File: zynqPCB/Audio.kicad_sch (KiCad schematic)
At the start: 67 parts, among them J2 AUDIO JACK, J3 AUDIO JACK, J4 AUDIO JACK, J5 JACK_TRS_4PINS, Q1 IRLML2502, Q2 IRLML2502, Q3 IRLML2502, Q4 IRLML2502, Q5 IRLML2502, Q6 IRLML2502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

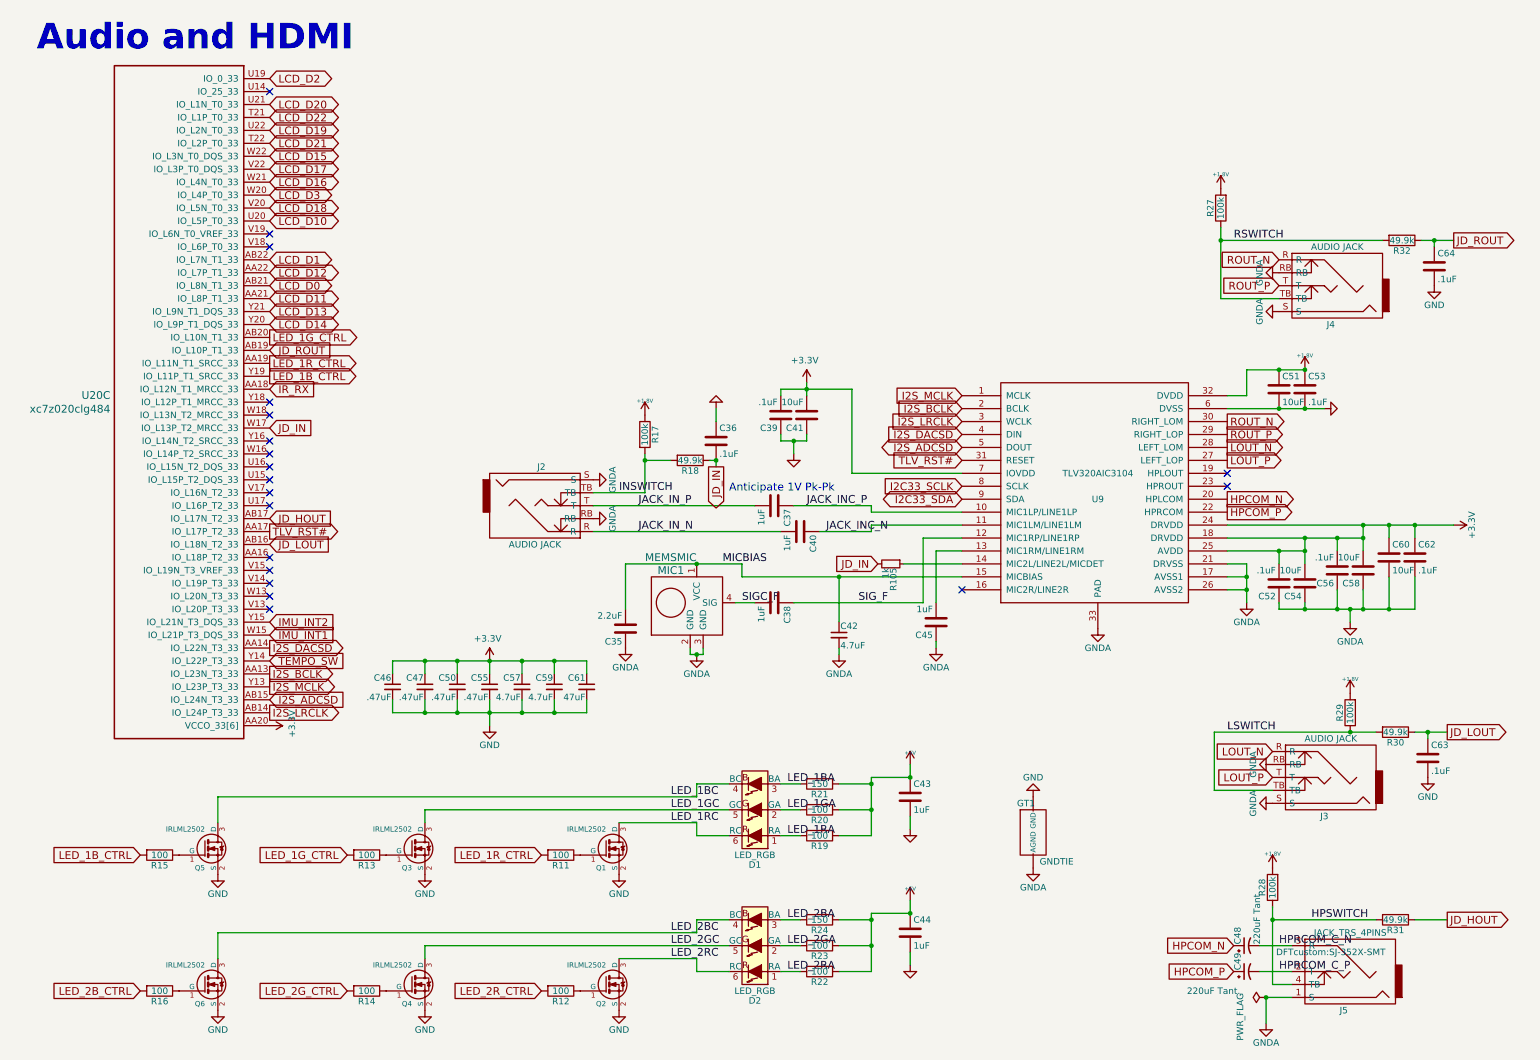
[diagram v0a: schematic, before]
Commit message: Update audio schematic
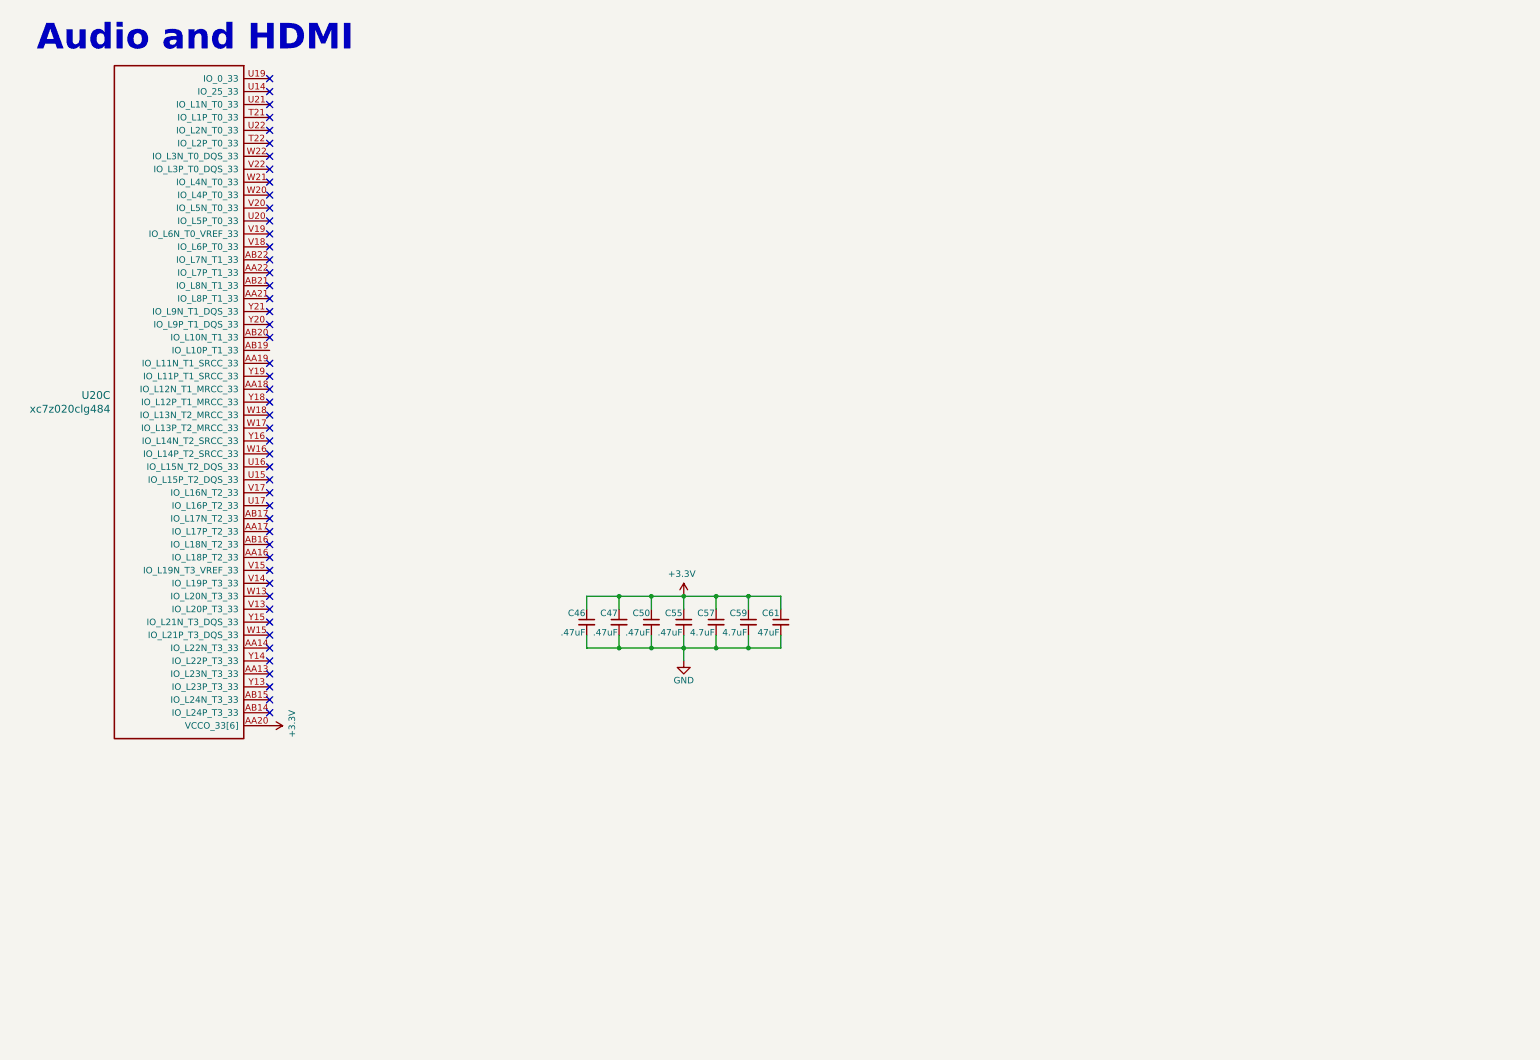
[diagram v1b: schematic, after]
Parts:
- removed C35: 2.2uF, Capacitor_SMD:C_0402_1005Metric, symbol Device:C
- removed C36, C39, C52, C53, C56, C62, C63, C64: .1uF, Capacitor_SMD:C_0402_1005Metric, symbol Device:C
- removed C37, C38, C40, C43, C44, C45: 1uF, Capacitor_SMD:C_0402_1005Metric, symbol Device:C
- removed C41, C51, C54, C58, C60: 10uF, Capacitor_SMD:C_0603_1608Metric, symbol Device:C
- removed C42: 4.7uF, Capacitor_SMD:C_0402_1005Metric, symbol Device:C_Small
- removed C48, C49: 220uF Tant., Capacitor_Tantalum_SMD:CP_EIA-3528-12_Kemet-T, symbol Device:CP1_Small
- removed D1, D2: LED_RGB, DFTcustom:PLCC6-SM-RGB-LED, symbol DFTBoard-rescue:LED_RGB-RESCUE-DFTBoard-
- removed GT1: GNDTIE, DFTcustom:gndtie, symbol DFTBoard-rescue:GNDTIE-
- removed J2, J3, J4: AUDIO JACK, DFTcustom:RA49C14B, symbol DFTBoard-rescue:JACK_TRS_5PINS
- removed J5: JACK_TRS_4PINS, DFTcustom:SJ-352X-SMT, symbol DFTBoard-rescue:JACK_TRS_4PINS
- removed MIC1: MEMSMIC, SPW2430HR5H-B:MIC_SPW2430HR5H-B, symbol DFTBoard-rescue:MEMSMIC
- removed Q1, Q2, Q3, Q4, Q5, Q6: IRLML2502, Package_TO_SOT_SMD:SOT-23, symbol DFTBoard-rescue:IRLML2502-
- removed R105: 1k, Resistor_SMD:R_0402_1005Metric, symbol Device:R_Small
- removed R11, R12, R13, R14, R15, R16, R19, R20, R22, R23: 100, Resistor_SMD:R_0402_1005Metric, symbol Device:R
- removed R17, R27, R28, R29: 100k, Resistor_SMD:R_0402_1005Metric, symbol Device:R
- removed R18, R30, R31, R32: 49.9k, Resistor_SMD:R_0402_1005Metric, symbol Device:R
- removed R21, R24: 150, Resistor_SMD:R_0402_1005Metric, symbol Device:R
- removed U9: TLV320AIC3104, Package_DFN_QFN:QFN-32-1EP_5x5mm_P0.5mm_EP3.65x3.65mm, symbol DFTBoard-rescue:TLV320AIC3104
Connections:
- net I2S_ADCSD: no longer names the net of U20.AB15 (IO_L24N_T3_33)
- net I2S_BCLK: no longer names the net of U20.AA13 (IO_L23N_T3_33)
- net I2S_DACSD: no longer names the net of U20.AA14 (IO_L22N_T3_33)
- net I2S_LRCLK: no longer names the net of U20.AB14 (IO_L24P_T3_33)
- net I2S_MCLK: no longer names the net of U20.Y13 (IO_L23P_T3_33)
- net IMU_INT1: no longer names the net of U20.W15 (IO_L21P_T3_DQS_33)
- net IMU_INT2: no longer names the net of U20.Y15 (IO_L21N_T3_DQS_33)
- net IR_RX: no longer names the net of U20.AA18 (IO_L12N_T1_MRCC_33)
- net JD_HOUT: no longer names the net of U20.AB17 (IO_L17N_T2_33)
- net JD_IN: no longer names the net of U20.W17 (IO_L13P_T2_MRCC_33)
- net JD_LOUT: no longer names the net of U20.AB16 (IO_L18N_T2_33)
- net JD_ROUT: no longer names the net of U20.AB19 (IO_L10P_T1_33)
- net LCD_D0: no longer names the net of U20.AB21 (IO_L8N_T1_33)
- net LCD_D1: no longer names the net of U20.AB22 (IO_L7N_T1_33)
- net LCD_D10: no longer names the net of U20.U20 (IO_L5P_T0_33)
- net LCD_D11: no longer names the net of U20.AA21 (IO_L8P_T1_33)
- net LCD_D12: no longer names the net of U20.AA22 (IO_L7P_T1_33)
- net LCD_D13: no longer names the net of U20.Y21 (IO_L9N_T1_DQS_33)
- net LCD_D14: no longer names the net of U20.Y20 (IO_L9P_T1_DQS_33)
- net LCD_D15: no longer names the net of U20.W22 (IO_L3N_T0_DQS_33)
- net LCD_D16: no longer names the net of U20.W21 (IO_L4N_T0_33)
- net LCD_D17: no longer names the net of U20.V22 (IO_L3P_T0_DQS_33)
- net LCD_D18: no longer names the net of U20.V20 (IO_L5N_T0_33)
- net LCD_D19: no longer names the net of U20.U22 (IO_L2N_T0_33)
- net LCD_D2: no longer names the net of U20.U19 (IO_0_33)
- net LCD_D20: no longer names the net of U20.U21 (IO_L1N_T0_33)
- net LCD_D21: no longer names the net of U20.T22 (IO_L2P_T0_33)
- net LCD_D22: no longer names the net of U20.T21 (IO_L1P_T0_33)
- net LCD_D3: no longer names the net of U20.W20 (IO_L4P_T0_33)
- net LED_1B_CTRL: no longer names the net of U20.Y19 (IO_L11P_T1_SRCC_33)
- net LED_1G_CTRL: no longer names the net of U20.AB20 (IO_L10N_T1_33)
- net LED_1R_CTRL: no longer names the net of U20.AA19 (IO_L11N_T1_SRCC_33)
- net TEMPO_SW: no longer names the net of U20.Y14 (IO_L22P_T3_33)
- net TLV_RST#: no longer names the net of U20.AA17 (IO_L17P_T2_33)
- no-connect marks 19 -> 49
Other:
- note removed: "Anticipate 1V Pk-Pk"
- moved on the sheet: C46, C47, C50, C55, C57, C59, C61
